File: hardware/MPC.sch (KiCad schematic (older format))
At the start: 14 parts, among them U10 CY7C1049DV33, U11 CY7C1049DV33, U4 EP4CE6F17, U9 SST39VF1681

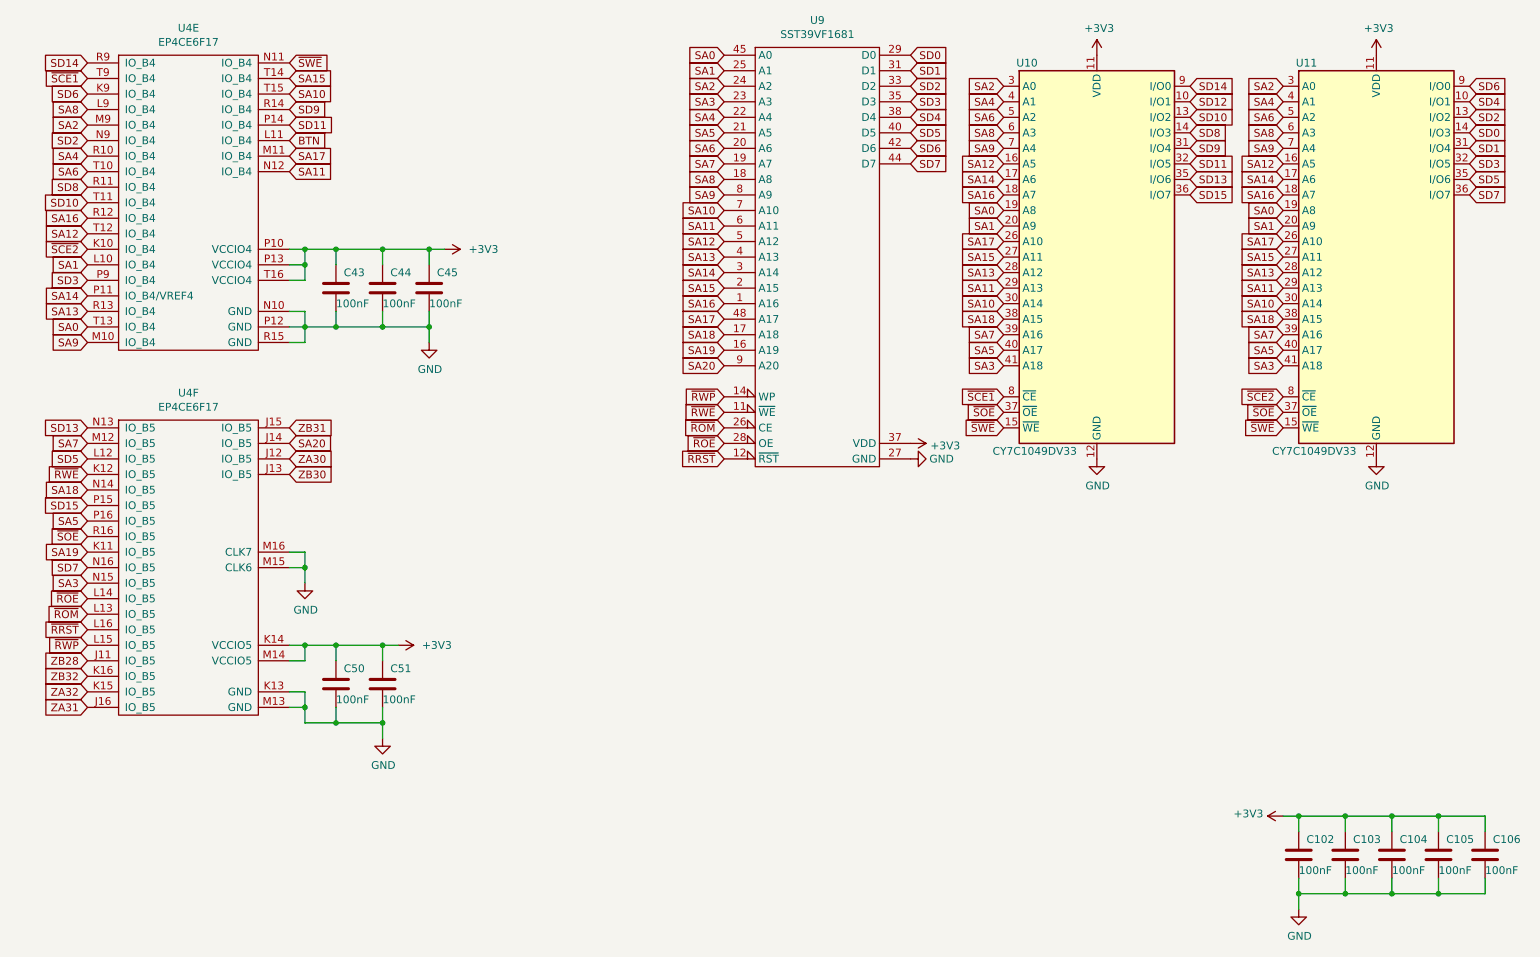
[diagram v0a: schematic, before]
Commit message: Обновлена схема:
1. Исправлена нумерация CS SRAM;
2. Исправлена нумерация сигналов для светодиодов.
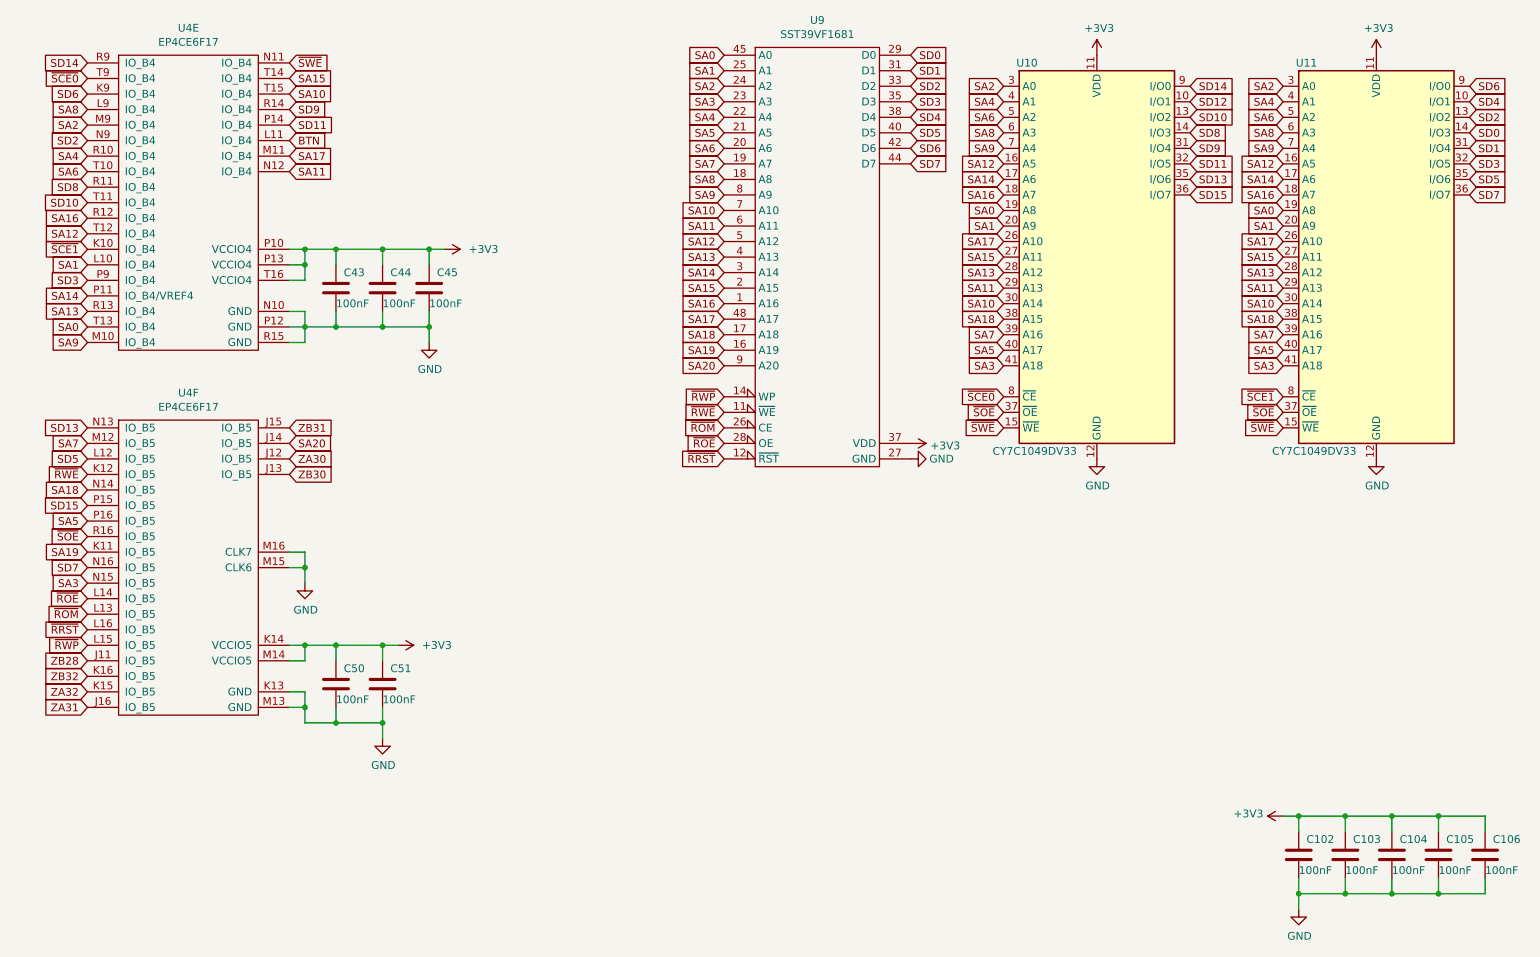
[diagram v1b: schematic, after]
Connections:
- net ~SCE2 is gone; now on net ~SCE1: U11.8 (~CE), U4.K10 (IO_B4)
- net ~SCE1: no longer U10.8 (~CE), U4.T9 (IO_B4)
- new net ~SCE0: U10.8 (~CE), U4.T9 (IO_B4)
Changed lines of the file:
@@
 ~ROM
 Text GLabel 7800 3000 0    50   Input ~ 0
-~SCE1
+~SCE0
 Text GLabel 7800 3100 0    50   Input ~ 0
 ~SOE
@@
 ~SWE
 Text GLabel 9600 3000 0    50   Input ~ 0
-~SCE2
+~SCE1
 Text GLabel 9600 3100 0    50   Input ~ 0
 ~SOE
@@
 SA6
 Text GLabel 1900 950  0    50   Input ~ 0
-~SCE1
+~SCE0
 Text GLabel 3200 850  2    50   Input ~ 0
 ~SWE
@@
 SD5
 Text GLabel 1900 2050 0    50   Input ~ 0
-~SCE2
+~SCE1
 Text GLabel 3200 1450 2    50   Input ~ 0
 SA17
